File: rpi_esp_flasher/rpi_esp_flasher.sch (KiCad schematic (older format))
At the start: 18 parts, among them J1 Raspberry_Pi_2_3, P1 ESP, SW1 PWR, U1 4427, U2 1117_5v_or_3v, U3 1k

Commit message: switch to LM5110
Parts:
- U1: value 4427 -> LM5110
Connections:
- net GND: now also U1.1 (NC)
- net GPIO2: now also U1.2 (INA)
- net at D6.2 (A), P1.4 (P4), U1.5 (OUTB): now also U1.7 (OUTA)
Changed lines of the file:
@@
 P 6050 2250
 F 0 "U1" H 6300 2500 60  0000 C CNN
-F 1 "4427" H 5800 2500 60  0000 C CNN
+F 1 "LM5110" H 5800 2500 60  0000 C CNN
 F 2 "SOIC-8_3.9x4.9mm_Pitch1.27mm" H 6050 2250 60  0000 C CNN
 F 3 "" H 6050 2250 60  0000 C CNN
@@
 Wire Wire Line
 	5150 4050 5150 3800
+$Comp
+L GND #PWR021
+U 1 1 5BDCA5E4
+P 5550 2100
+F 0 "#PWR021" H 5550 1850 50  0001 C CNN
+F 1 "GND" H 5550 1950 50  0000 C CNN
+F 2 "" H 5550 2100 50  0001 C CNN
+F 3 "" H 5550 2100 50  0001 C CNN
+	1    5550 2100
+	0    1    1    0
+$EndComp
+Text GLabel 5550 2200 0    60   Input ~ 0
+GPIO2
+Wire Wire Line
+	6600 2200 6750 2200
+Wire Wire Line
+	6750 2200 6750 2400
+Connection ~ 6750 2400
 $EndSCHEMATC

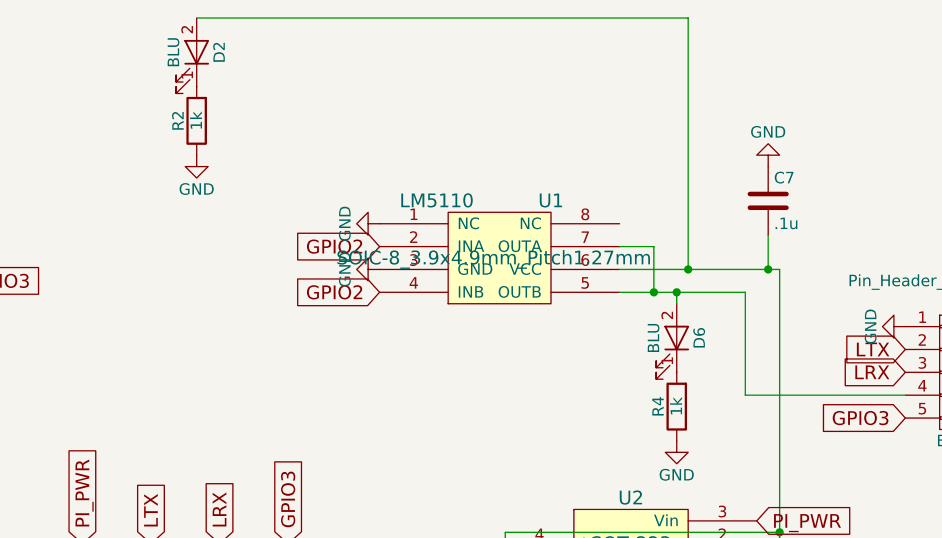
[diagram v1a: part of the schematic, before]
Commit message: Update revb with new switch
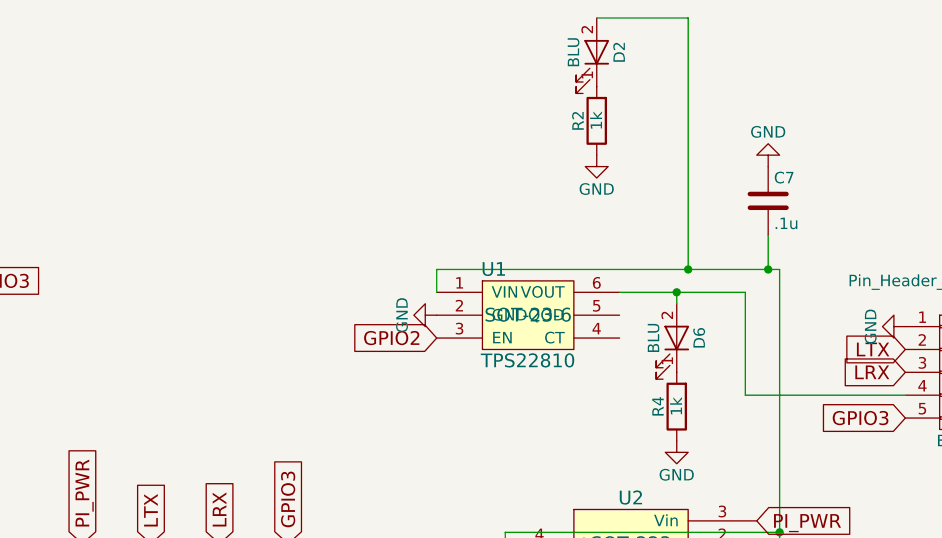
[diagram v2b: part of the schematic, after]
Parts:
- removed U1: LM5110, SOIC-8_3.9x4.9mm_Pitch1.27mm, symbol 4427
- added U1: TPS22810, SOT-23-6, symbol TPS22810-HIGH-SIDE-DRIVER
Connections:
- net GND: now also U1.2 (GND)
- net GPIO2: now also U1.3 (EN)
- net at C7.2, D2.2 (A), U2.2 (Vout)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: now also U1.1 (VIN)
- net at D6.2 (A), P1.4 (P4): now also U1.6 (VOUT)
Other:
- moved on the sheet: D2, R2
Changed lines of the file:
@@
 LIBS:vn7040-switch
 LIBS:ap1117sot223
+LIBS:tps22810-high-side-driver
 LIBS:rpi_esp_flasher-cache
 EELAYER 25 0
@@
 L LED-RESCUE-rpi_with_supply D2
 U 1 1 5AD03BF5
-P 4750 1350
-F 0 "D2" H 4750 1450 50  0000 C CNN
-F 1 "BLU" H 4750 1250 50  0000 C CNN
-F 2 "LED_0805" H 4750 1350 50  0001 C CNN
-F 3 "" H 4750 1350 50  0001 C CNN
-	1    4750 1350
+P 6500 1350
+F 0 "D2" H 6500 1450 50  0000 C CNN
+F 1 "BLU" H 6500 1250 50  0000 C CNN
+F 2 "LED_0805" H 6500 1350 50  0001 C CNN
+F 3 "" H 6500 1350 50  0001 C CNN
+	1    6500 1350
 	0    1    -1   0
 $EndComp
@@
 L R R2
 U 1 1 5AD04BA6
-P 4750 1650
-F 0 "R2" V 4830 1650 50  0000 C CNN
-F 1 "1k" V 4750 1650 50  0000 C CNN
-F 2 "R_0805" V 4680 1650 50  0001 C CNN
-F 3 "" H 4750 1650 50  0001 C CNN
-	1    4750 1650
+P 6500 1650
+F 0 "R2" V 6580 1650 50  0000 C CNN
+F 1 "1k" V 6500 1650 50  0000 C CNN
+F 2 "R_0805" V 6430 1650 50  0001 C CNN
+F 3 "" H 6500 1650 50  0001 C CNN
+	1    6500 1650
 	-1   0    0    1
 $EndComp
@@
 L GND #PWR010
 U 1 1 5AD05368
-P 4750 1800
-F 0 "#PWR010" H 4750 1550 50  0001 C CNN
-F 1 "GND" H 4750 1650 50  0000 C CNN
-F 2 "" H 4750 1800 50  0001 C CNN
-F 3 "" H 4750 1800 50  0001 C CNN
-	1    4750 1800
+P 6500 1800
+F 0 "#PWR010" H 6500 1550 50  0001 C CNN
+F 1 "GND" H 6500 1650 50  0000 C CNN
+F 2 "" H 6500 1800 50  0001 C CNN
+F 3 "" H 6500 1800 50  0001 C CNN
+	1    6500 1800
 	1    0    0    -1
 $EndComp
@@
 Text GLabel 4250 3500 1    60   Input ~ 0
 PI_PWR
-$Comp
-L 4427 U1
-U 1 1 5BD7DC6E
-P 6050 2250
-F 0 "U1" H 6300 2500 60  0000 C CNN
-F 1 "LM5110" H 5800 2500 60  0000 C CNN
-F 2 "SOIC-8_3.9x4.9mm_Pitch1.27mm" H 6050 2250 60  0000 C CNN
-F 3 "" H 6050 2250 60  0000 C CNN
-	1    6050 2250
-	1    0    0    -1
-$EndComp
 Text GLabel 3700 2350 2    60   Input ~ 0
 GPIO3
-Text GLabel 5550 2400 0    60   Input ~ 0
-GPIO2
 $Comp
 L R R5
@@
 Text GLabel 7850 2950 0    60   Input ~ 0
 GPIO3
-$Comp
-L GND #PWR014
-U 1 1 5BD7EA12
-P 5550 2300
-F 0 "#PWR014" H 5550 2050 50  0001 C CNN
-F 1 "GND" H 5550 2150 50  0000 C CNN
-F 2 "" H 5550 2300 50  0001 C CNN
-F 3 "" H 5550 2300 50  0001 C CNN
-	1    5550 2300
-	0    1    1    0
-$EndComp
 Text GLabel 7200 3400 2    60   Input ~ 0
 PI_PWR
@@
 $EndComp
 $Comp
-L GND #PWR015
+L GND #PWR014
 U 1 1 5BD780E6
 P 7200 3600
-F 0 "#PWR015" H 7200 3350 50  0001 C CNN
+F 0 "#PWR014" H 7200 3350 50  0001 C CNN
 F 1 "GND" H 7200 3450 50  0000 C CNN
 F 2 "" H 7200 3600 50  0001 C CNN
@@
 	0    -1   -1   0
 $EndComp
-Wire Wire Line
-	7300 2300 6600 2300
 Connection ~ 7300 3450
 Wire Wire Line
-	7250 2150 7250 2300
+	7250 2300 7250 2150
 Connection ~ 7250 2300
 $Comp
-L GND #PWR016
+L GND #PWR015
 U 1 1 5BD781C9
 P 7250 1850
-F 0 "#PWR016" H 7250 1600 50  0001 C CNN
+F 0 "#PWR015" H 7250 1600 50  0001 C CNN
 F 1 "GND" H 7250 1700 50  0000 C CNN
 F 2 "" H 7250 1850 50  0001 C CNN
@@
 Connection ~ 6850 2400
 Wire Wire Line
-	4750 1200 6900 1200
+	6500 1200 6900 1200
 Wire Wire Line
 	6900 1200 6900 2300
 Connection ~ 6900 2300
 $Comp
-L GND #PWR017
+L GND #PWR016
 U 1 1 5BD7940D
 P 6850 3050
-F 0 "#PWR017" H 6850 2800 50  0001 C CNN
+F 0 "#PWR016" H 6850 2800 50  0001 C CNN
 F 1 "GND" H 6850 2900 50  0000 C CNN
 F 2 "" H 6850 3050 50  0001 C CNN
@@
 LTX
 $Comp
-L GND #PWR018
+L GND #PWR017
 U 1 1 5BD7B792
 P 4650 5050
-F 0 "#PWR018" H 4650 4800 50  0001 C CNN
+F 0 "#PWR017" H 4650 4800 50  0001 C CNN
 F 1 "GND" H 4650 4900 50  0000 C CNN
 F 2 "" H 4650 5050 50  0001 C CNN
@@
 $EndComp
 $Comp
-L GND #PWR019
+L GND #PWR018
 U 1 1 5BD7B7F4
 P 4750 5050
-F 0 "#PWR019" H 4750 4800 50  0001 C CNN
+F 0 "#PWR018" H 4750 4800 50  0001 C CNN
 F 1 "GND" H 4750 4900 50  0000 C CNN
 F 2 "" H 4750 5050 50  0001 C CNN
@@
 $EndComp
 $Comp
-L GND #PWR020
+L GND #PWR019
 U 1 1 5BD7BBB9
 P 4850 5050
-F 0 "#PWR020" H 4850 4800 50  0001 C CNN
+F 0 "#PWR019" H 4850 4800 50  0001 C CNN
 F 1 "GND" H 4850 4900 50  0000 C CNN
 F 2 "" H 4850 5050 50  0001 C CNN
@@
 	5150 4050 5150 3800
 $Comp
-L GND #PWR021
+L GND #PWR020
 U 1 1 5BDCA5E4
-P 5550 2100
-F 0 "#PWR021" H 5550 1850 50  0001 C CNN
-F 1 "GND" H 5550 1950 50  0000 C CNN
-F 2 "" H 5550 2100 50  0001 C CNN
-F 3 "" H 5550 2100 50  0001 C CNN
-	1    5550 2100
+P 5800 2500
+F 0 "#PWR020" H 5800 2250 50  0001 C CNN
+F 1 "GND" H 5800 2350 50  0000 C CNN
+F 2 "" H 5800 2500 50  0001 C CNN
+F 3 "" H 5800 2500 50  0001 C CNN
+	1    5800 2500
 	0    1    1    0
 $EndComp
-Text GLabel 5550 2200 0    60   Input ~ 0
+Text GLabel 5800 2600 0    60   Input ~ 0
 GPIO2
-Wire Wire Line
-	6600 2200 6750 2200
-Wire Wire Line
-	6750 2200 6750 2400
-Connection ~ 6750 2400
+$Comp
+L TPS22810-HIGH-SIDE-DRIVER U1
+U 1 1 5BDCC08D
+P 6200 2500
+F 0 "U1" H 6050 2700 60  0000 C CNN
+F 1 "TPS22810" H 6200 2300 60  0000 C CNN
+F 2 "SOT-23-6" H 6200 2500 60  0000 C CNN
+F 3 "" H 6200 2500 60  0000 C CNN
+	1    6200 2500
+	1    0    0    -1
+$EndComp
+Wire Wire Line
+	5800 2300 7300 2300
+Wire Wire Line
+	5800 2300 5800 2400
 $EndSCHEMATC
